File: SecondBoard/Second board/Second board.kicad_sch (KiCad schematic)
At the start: 5 parts

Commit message: SecondBoard Rond m130
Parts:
- added J1, J2: Conn_01x04_Socket, TerminalBlock_Phoenix:TerminalBlock_Phoenix_MKDS-1,5-4_1x04_P5.00mm_Horizontal, symbol Connector:Conn_01x04_Socket
- GYBME1: footprint custom footprints:GY-BME280_P -> custom footprints:Sans titre
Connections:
- net +3.3V: now also J2.4 (Pin_4)
- net +5V: now also J1.4 (Pin_4)
- net GND: now also J1.3 (Pin_3), J2.3 (Pin_3)
- net at LightSensor1.4 (SCL), SPS30.3 (Pin_3), SecondBoardConnector1.8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: now also GYBME1.4 (SCK), J1.2 (Pin_2), J2.2 (Pin_2); no longer GYBME1.3 (SCL)
- net at LightSensor1.5 (SDA), SPS30.2 (Pin_2), SecondBoardConnector1.10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: now also GYBME1.6 (SDI), J1.1 (Pin_1), J2.1 (Pin_1); no longer GYBME1.4 (SDA)

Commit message: Plan de masse Update
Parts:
- added U1: ESP32-CAM, ESP32-CAM:ESP32-CAM, symbol ESP32-CAM:ESP32-CAM
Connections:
- net +5V: now also U1.5V
- net GND: now also U1.GND1
- net at SecondBoardConnector1.3: now also U1.U0T
- net at SecondBoardConnector1.5: now also U1.U0R

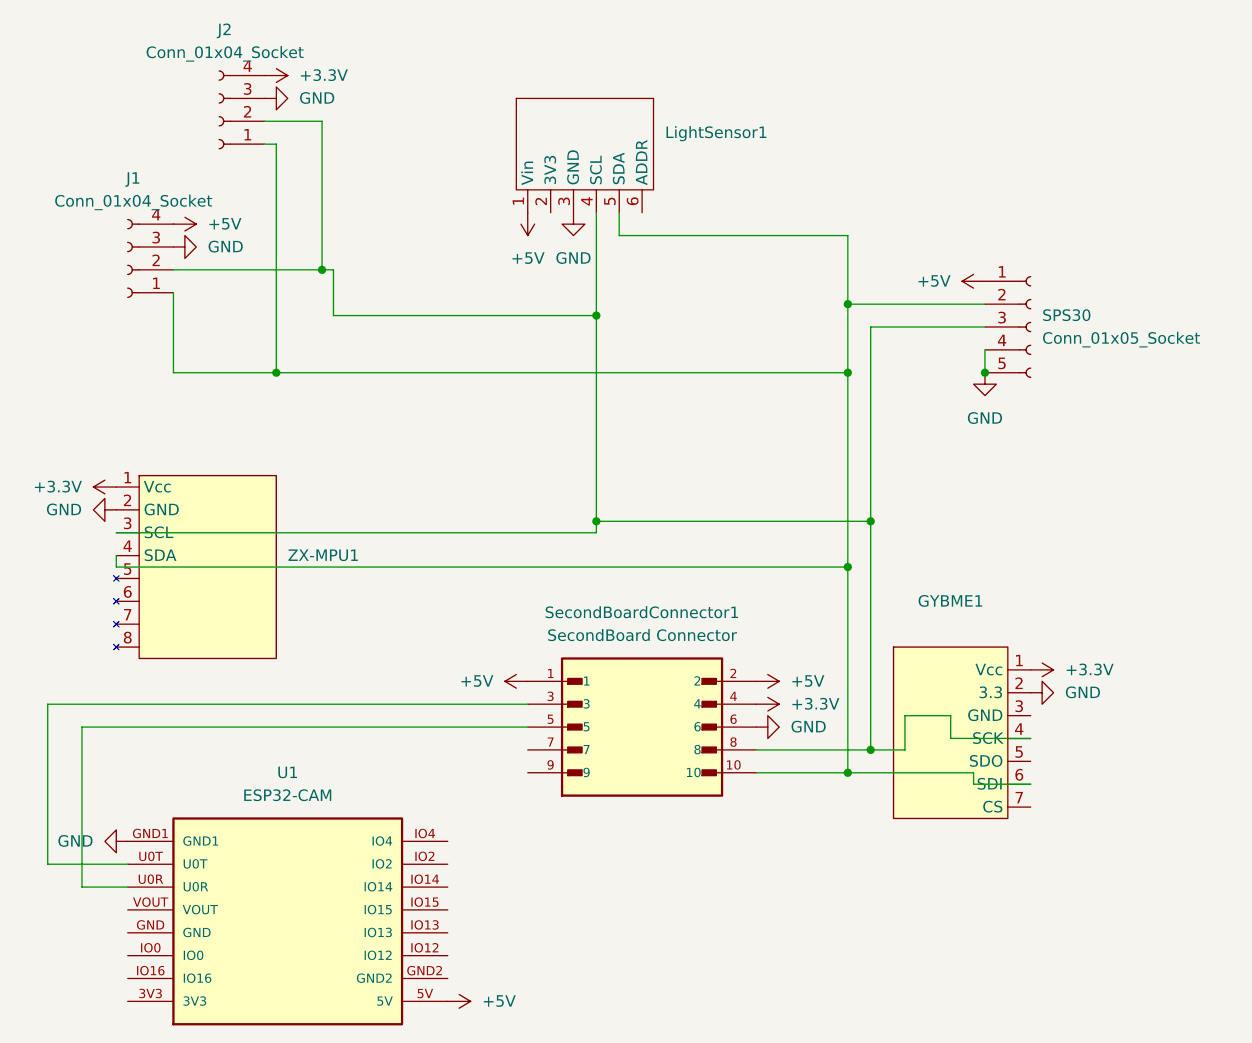
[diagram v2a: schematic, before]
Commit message: changement connecteur
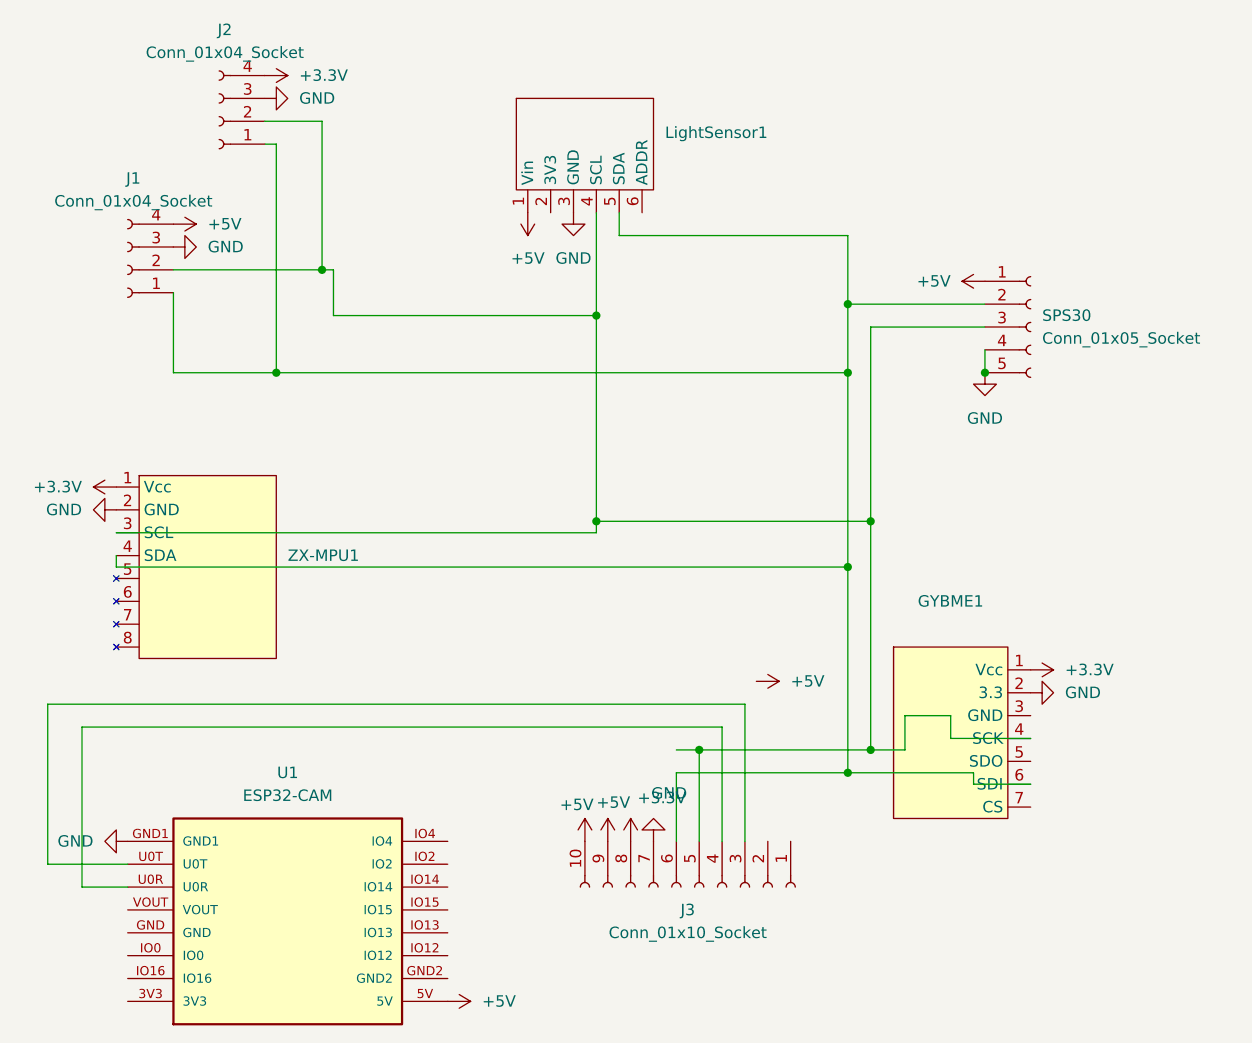
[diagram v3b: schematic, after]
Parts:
- removed SecondBoardConnector1: SecondBoard Connector, M50-3550542:HARWIN_M50-3550542, symbol M50-3550542:M50-3550542
- added J3: Conn_01x10_Socket, Connector_PinSocket_2.54mm:PinSocket_1x10_P2.54mm_Vertical, symbol Connector:Conn_01x10_Socket
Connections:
- net +3.3V: now also J3.8 (Pin_8)
- net +5V: now also J3.10 (Pin_10), J3.9 (Pin_9)
- net GND: now also J3.7 (Pin_7)
- net at GYBME1.4 (SCK), J1.2 (Pin_2), J2.2 (Pin_2)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: now also J3.5 (Pin_5)
- net at GYBME1.6 (SDI), J1.1 (Pin_1), J2.1 (Pin_1)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: now also J3.6 (Pin_6)
- net at U1.U0R: now also J3.4 (Pin_4)
- net at U1.U0T: now also J3.3 (Pin_3)

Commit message: finished version
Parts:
- I2C-1: renamed from J1; footprint TerminalBlock_Phoenix:TerminalBlock_Phoenix_MKDS-1,5-4_1x04_P5.00mm_Horizontal -> Connector_JST:JST_XH_B4B-XH-AM_1x04_P2.50mm_Vertical
- I2C-2: renamed from J2; footprint TerminalBlock_Phoenix:TerminalBlock_Phoenix_MKDS-1,5-4_1x04_P5.00mm_Horizontal -> Connector_JST:JST_XH_B4B-XH-AM_1x04_P2.50mm_Vertical
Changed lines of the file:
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@@
 		(dnp no)
 		(fields_autoplaced yes)
-		(property "Reference" "J1"
+		(property "Reference" "I2C-1"
 			(at 141.605 63.5 0)
 			(effects
@@
 			)
 		)
-		(property "Footprint" "TerminalBlock_Phoenix:TerminalBlock_Phoenix_MKDS-1,5-4_1x04_P5.00mm_Horizontal"
+		(property "Footprint" "Connector_JST:JST_XH_B4B-XH-AM_1x04_P2.50mm_Vertical"
 			(at 140.97 73.66 0)
 			(effects
@@
 			(project ""
 				(path "/9bbf387f-550e-4234-a71f-b6d3e1eade6b"
-					(reference "J1")
+					(reference "I2C-1")
 					(unit 1)
 				)
@@
 		(dnp no)
 		(fields_autoplaced yes)
-		(property "Reference" "J2"
+		(property "Reference" "I2C-2"
 			(at 151.765 46.99 0)
 			(effects
@@
 			)
 		)
-		(property "Footprint" "TerminalBlock_Phoenix:TerminalBlock_Phoenix_MKDS-1,5-4_1x04_P5.00mm_Horizontal"
+		(property "Footprint" "Connector_JST:JST_XH_B4B-XH-AM_1x04_P2.50mm_Vertical"
 			(at 151.13 57.15 0)
 			(effects
@@
 			(project "Second board"
 				(path "/9bbf387f-550e-4234-a71f-b6d3e1eade6b"
-					(reference "J2")
+					(reference "I2C-2")
 					(unit 1)
 				)
